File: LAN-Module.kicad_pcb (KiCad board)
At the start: 2 copper layers, 29 x 49 mm, 70 parts, among them J1 USB_B_Micro, J2 HR911105A, J3 Conn_Left, J4 ANT, J5 Conn_Right, Q1 2N7002, Q2 2N7002, SW1 RESET, U1 ESP32-U4WDH, U2 W25Q32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

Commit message: Layout PCB
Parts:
- J1: footprint Visclib:USB-B-MICRO-SMD -> Connector_USB:USB_Micro-B_Molex_47346-0001
- J3, J5: footprint Connector_PinHeader_2.54mm:PinHeader_1x16_P2.54mm_Vertical -> Visclib:ProtoCastellatedHeader_1x16
- U1: footprint Package_DFN_QFN:QFN-48-1EP_6x6mm_P0.4mm_EP4.3x4.3mm -> Visclib:ESP32-REDUCED
- moved SW1 45.8 mm to (45.5, 27.2), turned to 180 degrees
- moved C20 37.2 mm to (44.4, 50.4)
- moved C18 36.1 mm to (44.2, 54.4)
- moved C10 34.5 mm to (17.5, 37.2)
- moved R1 34.5 mm to (17.5, 39.2)
- moved D1 30.5 mm to (39.0, 50.8), turned to 90 degrees
- moved R6 29.5 mm to (41.4, 51.4)
- moved C21 28.8 mm to (40.8, 57.1), turned to -90 degrees
- moved R7 26.4 mm to (41.4, 52.6)
- moved R22 24.9 mm to (34.4, 46.8)
- moved R4 23.8 mm to (34.4, 45.0)
- moved C11 23.7 mm to (55.6, 35.8)
- moved Q2 19.9 mm to (24.5, 16.2)
- moved Q1 18.7 mm to (25.9, 20.3), turned to -90 degrees
- moved C6 18.4 mm to (43.4, 49.4)
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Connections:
- J3 pad 10: /VIN -> /IO5
- J3 pad 2: /U0TXD -> /IO16
- J3 pad 3: /U0RXD -> /IO12
- J3 pad 4: /EN -> /IO14
- J3 pad 5: /BOOT -> unconnected-(J3-Pad5)
- J3 pad 6: /IO32 -> /IO13
- J3 pad 7: /IO33 -> /IO15
- J3 pad 8: /IO34 -> /IO4
- J3 pad 9: /IO35 -> /IO2
- J5 pad 10: unconnected-(J5-Pad10) -> /S_VN
- J5 pad 11: unconnected-(J5-Pad11) -> /IO38
- J5 pad 12: unconnected-(J5-Pad12) -> /IO37
- J5 pad 13: unconnected-(J5-Pad13) -> /S_VP
- J5 pad 15: unconnected-(J5-Pad15) -> GND
- J5 pad 16: GND -> /VIN
- J5 pad 2: /IO15 -> /EN
- J5 pad 3: /IO14 -> /U0TXD
- J5 pad 4: /IO13 -> /U0RXD
- J5 pad 5: /IO12 -> /BOOT
- J5 pad 6: /IO16 -> /IO33
- J5 pad 7: /IO5 -> /IO32
- J5 pad 8: /IO4 -> /IO35
- J5 pad 9: /IO2 -> /IO34
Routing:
- net GND: track 53.5 -> 121.5 mm, vias 0 -> 3
- net /U0RXD: track 0.00 -> 43.8 mm, vias 0 -> 1
- net /U0TXD: track 0.00 -> 41.3 mm, vias 0 -> 1
- net /IO2: track 0.00 -> 33.2 mm, vias 0 -> 1
- net /BOOT: track 3.01 -> 34.3 mm, vias 0 -> 1
- net /IO13: track 0.00 -> 30.8 mm, vias 0 -> 1
- net /IO15: track 0.00 -> 29.5 mm, vias 0 -> 1
- net /S_VP: track 0.00 -> 28.2 mm, vias 0 -> 1
- net /IO37: track 0.00 -> 26.3 mm, vias 0 -> 1
- net /IO4: track 1.26 -> 26.9 mm
- net /IO38: track 0.00 -> 25.1 mm, vias 0 -> 1
- net /S_VN: track 0.00 -> 23.6 mm, vias 0 -> 1
- net /IO34: track 0.00 -> 21.0 mm, vias 0 -> 1
- net /IO35: track 0.00 -> 19.3 mm, vias 0 -> 1
- net /IO32: track 0.00 -> 17.4 mm, vias 0 -> 1
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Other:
- board size 29 x 49 mm -> 30.5 x 53.3 mm
- board text added: "3V3"
- board text added: "BOOT"
- board text added: "CT"
- board text added: "GND"
- board text added: "IO13"
- board text added: "IO15"
- board text added: "IO2"
- board text added: "IO32"
- board text added: "IO33"
- board text added: "IO34"
- board text added: "IO35"
- board text added: "IO37"
- board text added: "IO38"
- board text added: "IO4"
- board text added: "IO5"
- board text added: "RST"
- board text added: "RX"
- board text added: "RXN"
- board text added: "RXP"
- board text added: "TX"
- board text added: "TXN"
- board text added: "TXP"
- board text added: "VIN"
- board text added: "VN"
- board text added: "VP"

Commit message: Final routing and placement
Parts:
- removed C27: 100n, Capacitor_SMD:C_0603_1608Metric
- removed C4: 1u, Capacitor_SMD:C_0603_1608Metric
- removed C6: 10u, Capacitor_SMD:C_0603_1608Metric
- added F1: 1A, Fuse:Fuse_1206_3216Metric, F.Cu at (44.6, 59.0)
- added J10: ProtoCastellatedHeader, Visclib:ProtoCastellatedHeader_65mil, F.Cu at (22.9, 48.3)
- added J11: ProtoCastellatedHeader, Visclib:ProtoCastellatedHeader_65mil, F.Cu at (22.9, 50.8)
- added J12: ProtoCastellatedHeader, Visclib:ProtoCastellatedHeader_65mil, F.Cu at (22.9, 53.3)
- added J13: ProtoCastellatedHeader, Visclib:ProtoCastellatedHeader_65mil, F.Cu at (22.9, 55.9)
- added J14: ProtoCastellatedHeader, Visclib:ProtoCastellatedHeader_65mil, F.Cu at (22.9, 58.4)
- added J15: ProtoCastellatedHeader, Visclib:ProtoCastellatedHeader_65mil, F.Cu at (48.3, 55.9)
- added J16: ProtoCastellatedHeader, Visclib:ProtoCastellatedHeader_65mil, F.Cu at (22.9, 61.0)
- added J17: ProtoCastellatedHeader, Visclib:ProtoCastellatedHeader_65mil, F.Cu at (48.3, 30.5)
- added J18: ProtoCastellatedHeader, Visclib:ProtoCastellatedHeader_65mil, F.Cu at (48.3, 33.0)
- added J19: ProtoCastellatedHeader, Visclib:ProtoCastellatedHeader_65mil, F.Cu at (48.3, 35.6)
- added J20: ProtoCastellatedHeader, Visclib:ProtoCastellatedHeader_65mil, F.Cu at (48.3, 38.1)
- added J21: ProtoCastellatedHeader, Visclib:ProtoCastellatedHeader_65mil, F.Cu at (48.3, 40.6)
- added J22: ProtoCastellatedHeader, Visclib:ProtoCastellatedHeader_65mil, F.Cu at (48.3, 43.2)
- added J23: ProtoCastellatedHeader, Visclib:ProtoCastellatedHeader_65mil, F.Cu at (48.3, 45.7)
- added J24: ProtoCastellatedHeader, Visclib:ProtoCastellatedHeader_65mil, F.Cu at (48.3, 48.3)
- added J25: ProtoCastellatedHeader, Visclib:ProtoCastellatedHeader_65mil, F.Cu at (48.3, 50.8)
- added J26: ProtoCastellatedHeader, Visclib:ProtoCastellatedHeader_65mil, F.Cu at (48.3, 53.3)
- added J27: ProtoCastellatedHeader, Visclib:ProtoCastellatedHeader_65mil, F.Cu at (48.3, 58.4)
- added J28: ProtoCastellatedHeader, Visclib:ProtoCastellatedHeader_65mil, F.Cu at (48.3, 61.0)
- added J6: ProtoCastellatedHeader, Visclib:ProtoCastellatedHeader_65mil, F.Cu at (22.9, 38.1)
- added J7: ProtoCastellatedHeader, Visclib:ProtoCastellatedHeader_65mil, F.Cu at (22.9, 40.6)
- added J8: ProtoCastellatedHeader, Visclib:ProtoCastellatedHeader_65mil, F.Cu at (22.9, 43.2)
- added J9: ProtoCastellatedHeader, Visclib:ProtoCastellatedHeader_65mil, F.Cu at (22.9, 45.7)
- J3: value Conn_Left -> ProtoCastellatedHeader; footprint Visclib:ProtoCastellatedHeader_1x16 -> Visclib:ProtoCastellatedHeader_65mil
- J4: value ANT -> ProtoCastellatedHeader; footprint Connector_Coaxial:U.FL_Hirose_U.FL-R-SMT-1_Vertical -> Visclib:ProtoCastellatedHeader_65mil
- J5: value Conn_Right -> ProtoCastellatedHeader; footprint Visclib:ProtoCastellatedHeader_1x16 -> Visclib:ProtoCastellatedHeader_65mil
- moved J4 37.7 mm to (22.9, 33.0), turned to 180 degrees
- moved J5 28.4 mm to (22.9, 35.6), turned to 180 degrees
- moved R5 22.9 mm to (26.0, 49.4), turned to -90 degrees
- moved R21 19.2 mm to (46.0, 31.6), turned to -90 degrees
- moved SW1 17.9 mm to (27.6, 27.0)
- moved Q2 15.3 mm to (26.0, 31.4)
- moved R1 12.3 mm to (23.2, 28.4)
- moved D2 12.2 mm to (43.0, 27.2), turned to 180 degrees
- moved C10 11.9 mm to (23.2, 26.8)
- moved Q1 11.8 mm to (30.0, 31.4), turned to 0 degrees
- moved R23 11.6 mm to (28.0, 34.6), turned to -90 degrees
- moved C11 11.6 mm to (44.0, 35.8), turned to 180 degrees
- moved R24 10.3 mm to (26.4, 34.6), turned to -90 degrees
- moved R19 9.75 mm to (47.0, 28.2), turned to 180 degrees
- moved C21 7.98 mm to (45.5, 50.7), turned to 90 degrees
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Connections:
- net Net-(C20-Pad2) renamed /SW
- net Net-(J1-Pad2) renamed /USB_N
- net Net-(J1-Pad3) renamed /USB_P
- net Net-(Q1-Pad1) renamed /RTS
- net Net-(Q1-Pad3) renamed /DTR
- net Net-(R6-Pad2) renamed /FB
- C18 pad 1: VDD -> Net-(C17-Pad1)
- D2 pad 1: VDD -> /VIN
- J4 pad 1: Net-(J4-Pad1) -> /EN
- J5 pad 1: /3V3 -> /BOOT
- L3 pad 1: VDD -> +3V3
- R10 pad 1: VDD -> +3V3
- R9 pad 1: VDD -> +3V3
- U1 pad 2: Net-(J4-Pad1) -> unconnected-(U1-Pad2)
- U3 pad 4: VDD -> Net-(C17-Pad1)
- U3 pad 5: VDD -> Net-(C17-Pad1)
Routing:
- net GND: track 121.5 -> 312.5 mm, vias 3 -> 24
- net +3V3: track 22.2 -> 128.5 mm, vias 0 -> 7
- net /VIN: track 0.00 -> 36.2 mm
- net /IO14: track 0.98 -> 32.2 mm
- net /IO12: track 0.98 -> 28.6 mm, vias 1 -> 2
- net /MDI1_N: track 29.1 -> 10.9 mm
- net /BOOT: track 34.3 -> 16.6 mm, vias 1 -> 0
- net /USB_P: track 0.00 -> 15.8 mm, vias 0 -> 2
- net /USB_N: track 0.00 -> 15.3 mm, vias 0 -> 2
- net /DTR: track 0.00 -> 15.0 mm
- net /RTS: track 0.00 -> 14.8 mm
- net /MDI0_CT: track 27.8 -> 14.2 mm
- net VBUS: track 0.00 -> 13.1 mm
- net /SDD0: track 0.00 -> 13.0 mm, vias 0 -> 2
- net /IO13: track 30.8 -> 18.1 mm
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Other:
- board size 30.5 x 53.3 mm -> 28.6 x 53.3 mm
- board text added: "40V MAX"
- board text added: "ESP32 ETH r1"
- board text added: "ETHERNET"
- board text added: "GPIO"
- board text added: "IO12"
- board text added: "IO14"
- board text added: "LNA ADC"
- board text added: "UART"
- board text added: "USB-UART"
- board text added: "jared.geek.nz"
- board text removed: "BOOT"
- board text removed: "CT"
- board text removed: "IO13"
- board text removed: "IO15"
- board text removed: "RST"
- board text removed: "RXN"
- board text removed: "RXP"
- board text removed: "TXN"
- board text removed: "TXP"

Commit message: Address TODOs
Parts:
- D1: value FM240W -> PMEG6020ER,115
- D2: value FM240W -> ?
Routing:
- net +3V3: track 128.5 -> 135.5 mm, vias 7 -> 8

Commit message: Generate gerbers r1
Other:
- board text added: "JLCJLCJLCJLC"
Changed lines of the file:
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@@
     (pad_to_mask_clearance 0)
     (pcbplotparams
-      (layerselection 0x00010fc_ffffffff)
+      (layerselection 0x00010f0_ffffffff)
       (disableapertmacros false)
-      (usegerberextensions false)
-      (usegerberattributes true)
+      (usegerberextensions true)
+      (usegerberattributes false)
       (usegerberadvancedattributes true)
-      (creategerberjobfile true)
+      (creategerberjobfile false)
       (svguseinch false)
       (svgprecision 6)
@@
       (psnegative false)
       (psa4output false)
-      (plotreference true)
+      (plotreference false)
       (plotvalue true)
       (plotinvisibletext false)
       (sketchpadsonfab false)
-      (subtractmaskfromsilk false)
+      (subtractmaskfromsilk true)
       (outputformat 1)
       (mirror false)
-      (drillshape 1)
+      (drillshape 0)
       (scaleselection 1)
-      (outputdirectory "")
+      (outputdirectory "Gerbers_r1")
     )
   )
@@
     (effects (font (size 0.5 0.5) (thickness 0.125)) (justify right))
   )
+  (gr_text "JLCJLCJLCJLC" (at 35.2 66.8) (layer "F.SilkS")
+    (effects (font (size 0.8 0.8) (thickness 0.15)))
+  )
   (gr_text "GND" (at 21.59 62.23 180) (layer "F.SilkS")

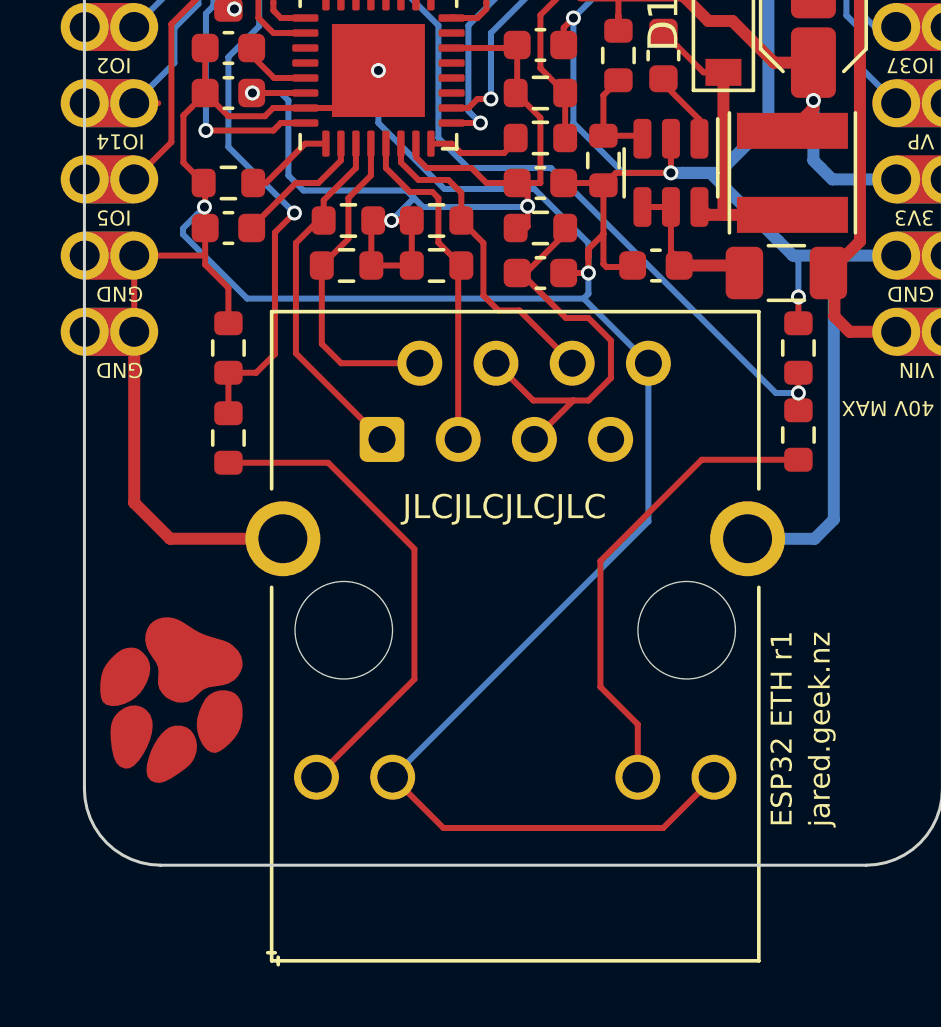
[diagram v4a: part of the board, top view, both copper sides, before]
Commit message: HW REV: Fix stability issue
Important change required to ensure stability across different types of ethernet switches.

I had only tested this with a TP-LINK switch, but the design did not work with other switches, and the reference schematic does NOT specify that the CT/termination resistors should be tied to 3.3V. Instead they should be coupled to GND through a capacitor (of unspecified value).
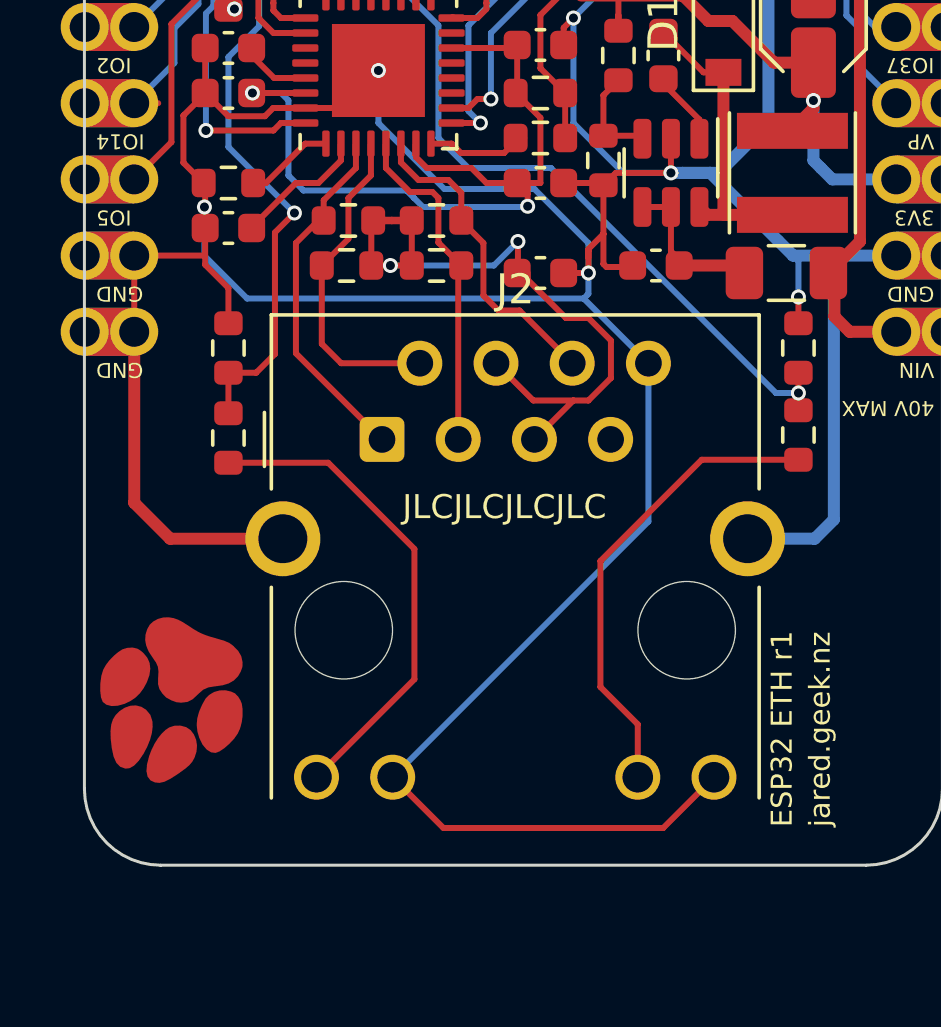
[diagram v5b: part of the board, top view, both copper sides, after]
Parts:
- removed R25: 0R, Resistor_SMD:R_0603_1608Metric
- J2: footprint Connector_RJ:RJ45_Hanrun_HR911105A -> Visclib:RJ45_Hanrun_HR911105A_Horizontal
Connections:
- J2 pad 11: /ETH_LED1 -> GND
- J2 pad 12: GND -> /ETH_LED1
- J2 pad SH: (no net) -> GND
- R13 pad 1: /LAN_3P3V -> /MDI0_CT
- R14 pad 1: /LAN_3P3V -> /MDI0_CT
- R17 pad 1: /LAN_3P3V -> /MDI0_CT
- R18 pad 1: /LAN_3P3V -> /MDI0_CT
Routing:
- net /MDI0_CT: track 14.2 -> 23.3 mm, vias 0 -> 2
- net /LAN_3P3V: track 35.1 -> 27.7 mm, vias 3 -> 2
- net GND: track 312.5 -> 311.9 mm
